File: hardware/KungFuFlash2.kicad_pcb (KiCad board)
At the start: 2 copper layers, 60.6 x 62 mm, 53 parts, among them J1 SWD, J2 USB_B_Micro, J3 Wifi, Q1 BC817, SW1 Reset, SW2 Menu, SW3 Special, U1 C64-Exp-Port, U2 AMS1117-3.3, U3 STM32H7B0VBTx, Y1 25MHz

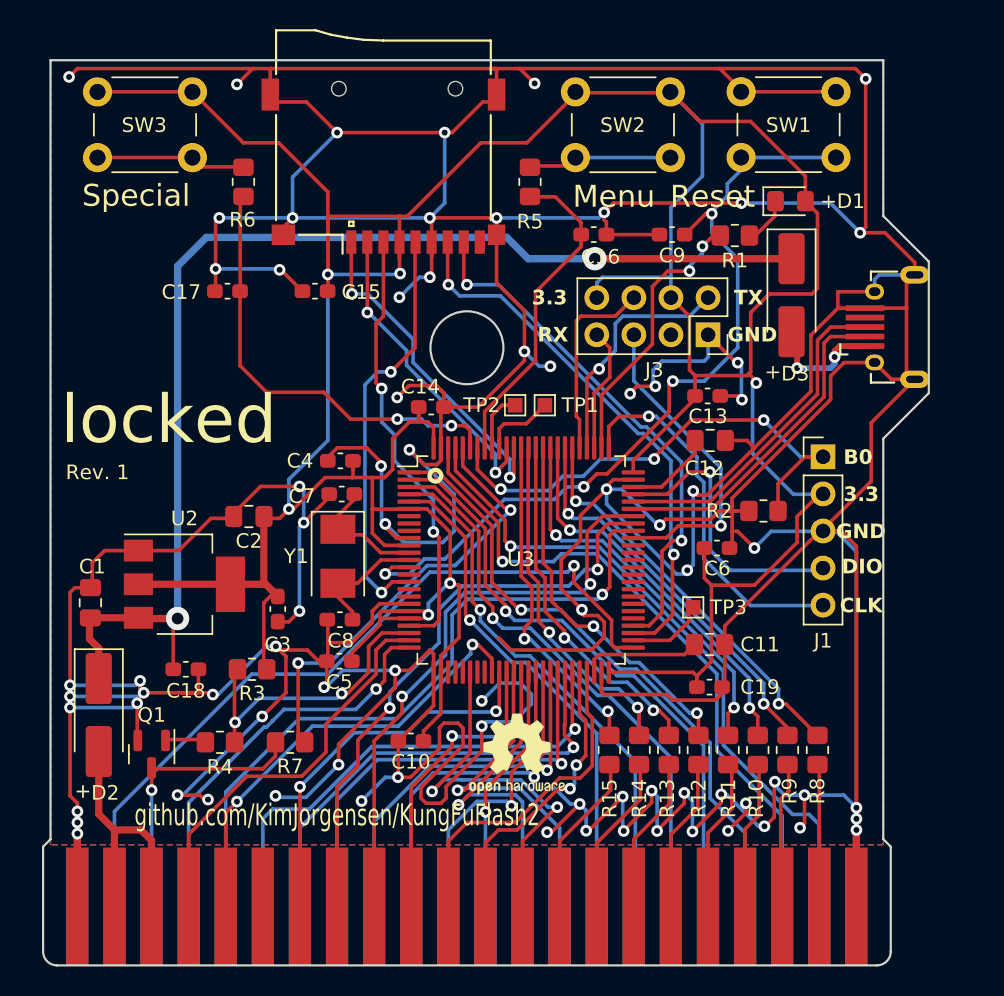
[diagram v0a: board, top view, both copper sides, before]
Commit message: Adapting board for JLCPCB ordering
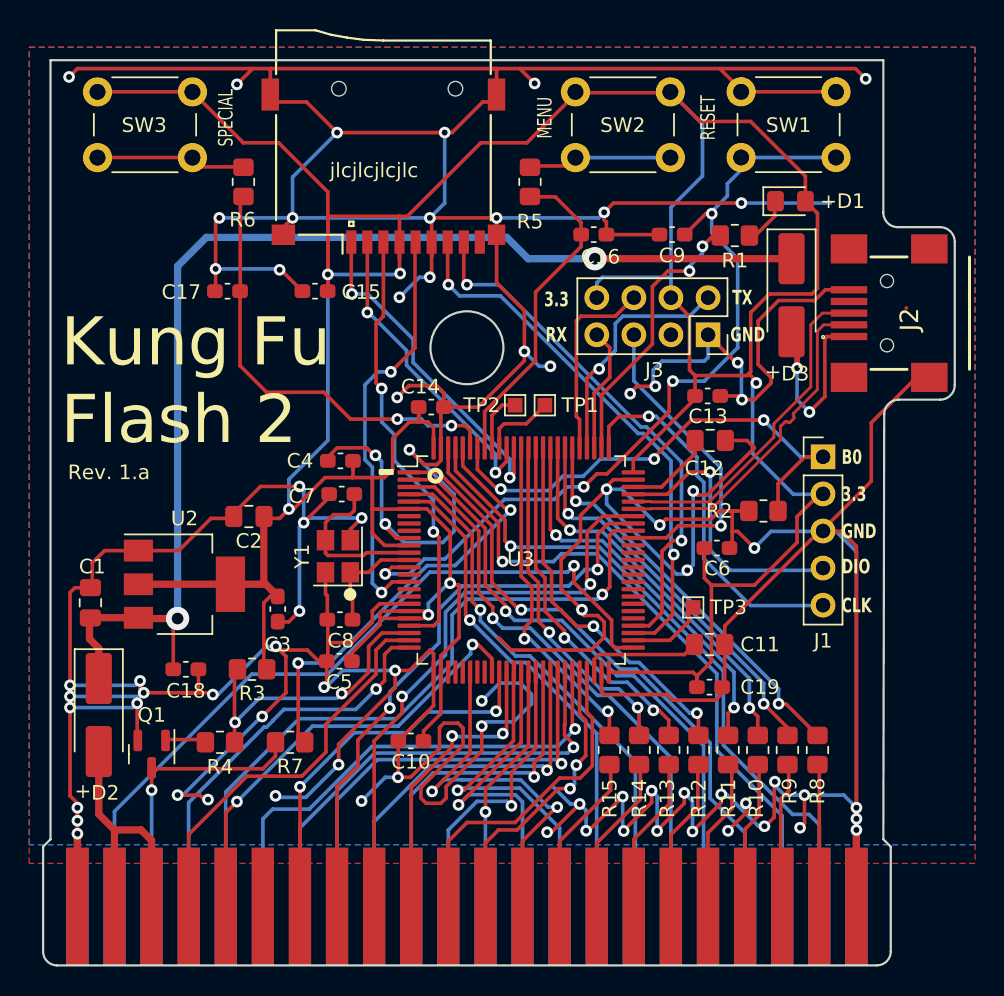
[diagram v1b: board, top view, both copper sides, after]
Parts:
- removed REF**: OSHW-Logo2_7.3x6mm_SilkScreen, Symbol:OSHW-Logo2_7.3x6mm_SilkScreen
- C1, C2: value 10u -> 10uF
- C10, C13, C14, C15, C16, C17, C18, C19, C3, C4, C5, C6, C9: value 100n -> 100nF
- C11, C12: value 2.2u -> 2.2uF
- C7, C8: value 20p -> 20pF
- J2: footprint KungFuFlash2:Conn_USBmicro-B_ebay-side_TH -> mod:Conn_USBmini_reichelt
- Y1: value 25MHz -> 25 MHz; footprint Crystal:Crystal_SMD_5032-2Pin_5.0x3.2mm -> Crystal:Crystal_SMD_3225-4Pin_3.2x2.5mm
- moved J2 5.58 mm to (130.1, 85.5)
- turned Y1 to 90 degrees
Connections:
- net /USB_DM renamed /USB_D-
- net /USB_DP renamed /USB_D+
- Y1 pad 1: Net-(U3-PH0) -> Net-(U3-PH1)
- Y1 pad 2: Net-(U3-PH1) -> GND
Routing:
- net GND: track 705.4 -> 659.5 mm
- net +5C: track 7.91 -> 12.6 mm
- net Net-(U3-PH0): track 8.27 -> 11.4 mm
- net Net-(U3-PH1): track 8.44 -> 7.68 mm
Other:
- board size 60.6 x 62 mm -> 62.4 x 62 mm
- board text added: "Board adapted from: https://github.com/KimJorgensen/KungFuFlash2"
- board text added: "Kung Fu Flash 2"
- board text added: "MENU"
- board text added: "RESET"
- board text added: "Rev. 1.a"
- board text added: "SPECIAL"
- board text added: "jlcjlcjlcjlc"
- board text removed: "Menu"
- board text removed: "Reset"
- board text removed: "Rev. 1"
- board text removed: "Special"
- board text removed: "github.com/KimJorgensen/KungFuFlash2"
- board text removed: "locked"
